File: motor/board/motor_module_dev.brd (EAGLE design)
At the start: 44.4 x 51.7 mm, 74 parts, among them IC6 LTC6088, IC7 DRV8833RTY

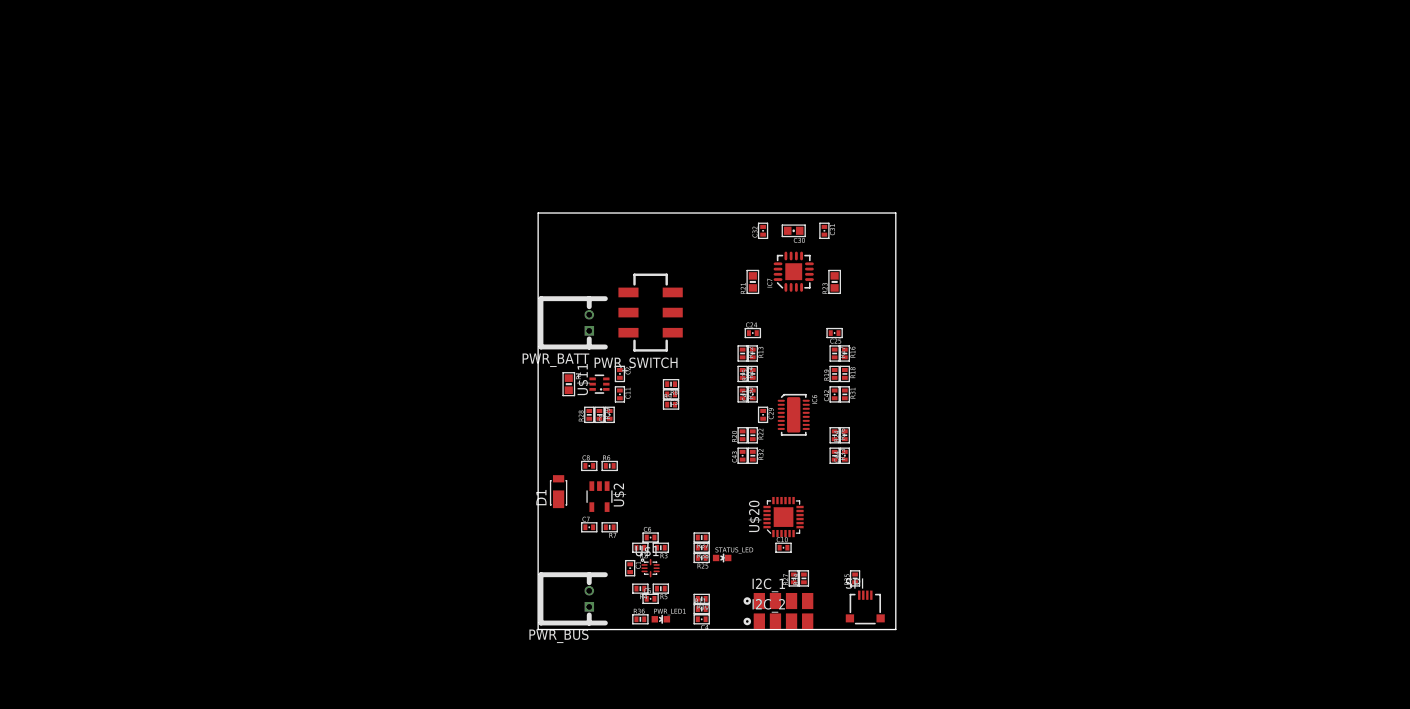
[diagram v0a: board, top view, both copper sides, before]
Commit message: Switched I2C and Charge pins for better Arduino compatability. Adding dev version
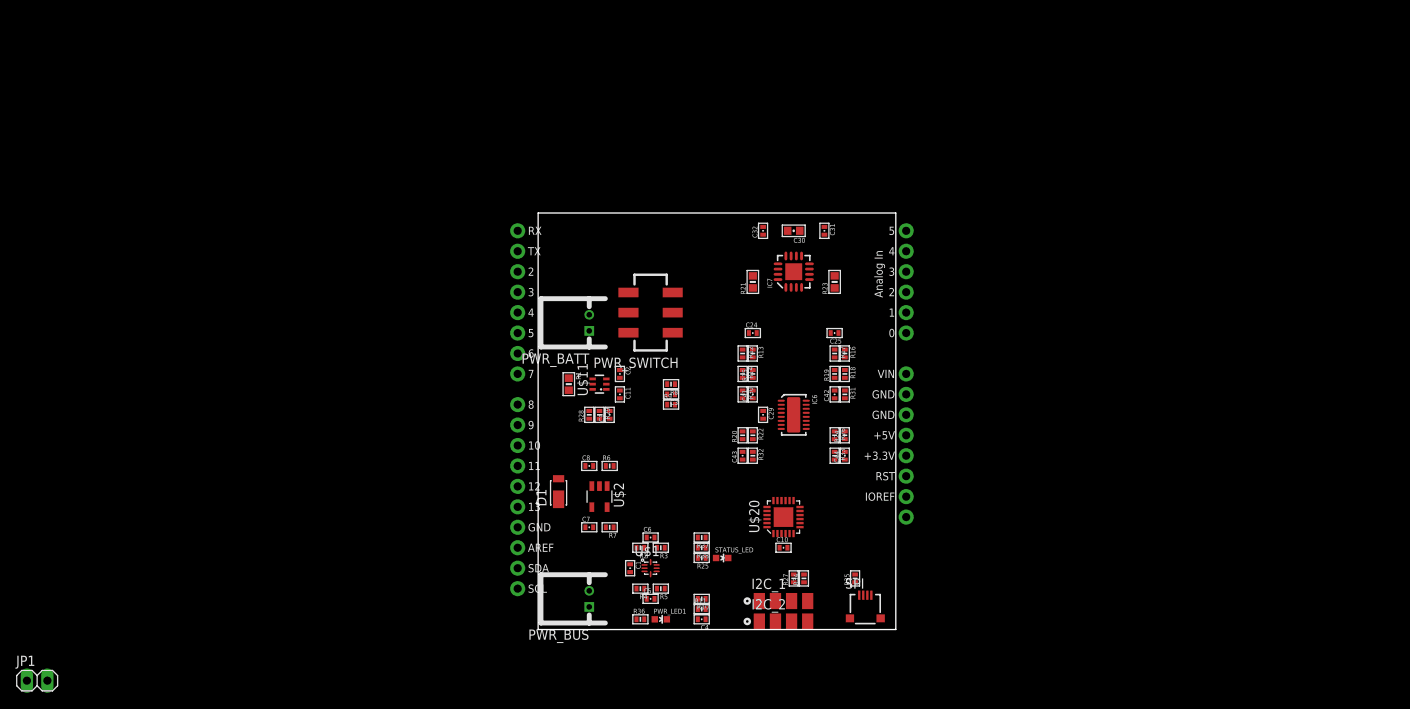
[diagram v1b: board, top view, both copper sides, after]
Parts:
- added JP1: (no value), pinhead:1X02
- added U$27: ARDUINO_R3_SHIELD, SparkFun-Boards:UNO_R3_SHIELD
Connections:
- new net N$10: JP1.2, U$27.5V
- net GND: now also U$27.GND@0, U$27.GND@1, U$27.GND@2
- net I2C_SCL: now also U$27.SCL
- net I2C_SDA: now also U$27.SDA
- net SPI_SS: now also U$27.D10
- net V_BUS: now also JP1.1
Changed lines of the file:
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@@
 <element name="R38" library="biomimetic" package="0402-RES" value="4.7k" x="20.32" y="10.16" rot="R180"/>
 <element name="C11" library="biomimetic" package="0402-CAP" value="100nF" x="10.16" y="29.21" rot="R270"/>
+<element name="U$27" library="SparkFun-Boards" package="UNO_R3_SHIELD" value="ARDUINO_R3_SHIELD" x="-5.08" y="-5.08"/>
+<element name="JP1" library="pinhead" package="1X02" value="" x="-62.23" y="-6.35"/>
 </elements>
 <signals>
@@
 <contactref element="I2C_2" pad="2"/>
 <contactref element="C11" pad="1"/>
+<contactref element="U$27" pad="GND@2"/>
+<contactref element="U$27" pad="GND@1"/>
+<contactref element="U$27" pad="GND@0"/>
 <wire x1="27.94" y1="50.0126" x2="31.0007" y2="49.53" width="0" layer="19" extent="1-1"/>
 <wire x1="31.425" y1="46.4" x2="31.0007" y2="49.53" width="0" layer="19" extent="1-1"/>
@@
 <wire x1="30.9626" y1="10.16" x2="29.48" y2="3.54" width="0" layer="19" extent="1-1"/>
 <wire x1="30.73" y1="11.92" x2="30.9626" y2="10.16" width="0" layer="19" extent="1-1"/>
+<wire x1="45.72" y1="26.67" x2="6.35" y2="37.1" width="0" layer="19" extent="1-1"/>
+<wire x1="45.72" y1="29.21" x2="45.72" y2="26.67" width="0" layer="19" extent="1-1"/>
+<wire x1="-2.54" y1="12.7" x2="45.72" y2="26.67" width="0" layer="19" extent="1-1"/>
 </signal>
 <signal name="N$1">
@@
 <contactref element="C1" pad="1"/>
 <contactref element="U$1" pad="6"/>
-<wire x1="14.72" y1="7.62" x2="19.8374" y2="3.81" width="0" layer="19" extent="1-1"/>
-<wire x1="13.22" y1="7.62" x2="14.72" y2="7.62" width="0" layer="19" extent="1-1"/>
-<wire x1="11.43" y1="8.1026" x2="13.22" y2="7.62" width="0" layer="19" extent="1-1"/>
+<contactref element="JP1" pad="1"/>
+<wire x1="2.54" y1="16.18" x2="-63.5" y2="-6.35" width="0" layer="19" extent="1-1"/>
+<wire x1="6.67" y1="15.204" x2="2.54" y2="16.18" width="0" layer="19" extent="1-1"/>
+<wire x1="5.8674" y1="12.7" x2="6.67" y2="15.204" width="0" layer="19" extent="1-1"/>
+<wire x1="11.43" y1="8.1026" x2="5.8674" y2="12.7" width="0" layer="19" extent="1-1"/>
+<wire x1="13.22" y1="7.62" x2="11.43" y2="8.1026" width="0" layer="19" extent="1-1"/>
+<wire x1="14.72" y1="7.62" x2="13.22" y2="7.62" width="0" layer="19" extent="1-1"/>
 <wire x1="6.35" y1="4.81" x2="11.43" y2="8.1026" width="0" layer="19" extent="1-1"/>
-<wire x1="5.8674" y1="12.7" x2="11.43" y2="8.1026" width="0" layer="19" extent="1-1"/>
-<wire x1="6.67" y1="15.204" x2="5.8674" y2="12.7" width="0" layer="19" extent="1-1"/>
-<wire x1="2.54" y1="16.18" x2="6.67" y2="15.204" width="0" layer="19" extent="1-1"/>
+<wire x1="19.8374" y1="3.81" x2="14.72" y2="7.62" width="0" layer="19" extent="1-1"/>
 </signal>
 <signal name="N$4">
@@
 <contactref element="I2C_1" pad="3"/>
 <contactref element="U$20" pad="17"/>
+<contactref element="U$27" pad="SCL"/>
 <wire x1="31.75" y1="5.8674" x2="29.73" y2="16.02" width="0" layer="19" extent="1-1"/>
 <wire x1="31.48" y1="3.54" x2="31.75" y2="5.8674" width="0" layer="19" extent="1-1"/>
 <wire x1="31.48" y1="1" x2="31.48" y2="3.54" width="0" layer="19" extent="1-1"/>
+<wire x1="-2.54" y1="5.08" x2="29.73" y2="16.02" width="0" layer="19" extent="1-1"/>
 </signal>
 <signal name="I2C_SDA">
@@
 <contactref element="R34" pad="1"/>
 <contactref element="U$20" pad="18"/>
+<contactref element="U$27" pad="SDA"/>
 <wire x1="33.02" y1="5.8674" x2="29.23" y2="16.02" width="0" layer="19" extent="1-1"/>
 <wire x1="33.48" y1="3.54" x2="33.02" y2="5.8674" width="0" layer="19" extent="1-1"/>
 <wire x1="33.48" y1="1" x2="33.48" y2="3.54" width="0" layer="19" extent="1-1"/>
+<wire x1="-2.54" y1="7.62" x2="29.23" y2="16.02" width="0" layer="19" extent="1-1"/>
 </signal>
 <signal name="SPI_SS">
@@
 <contactref element="SPI" pad="1"/>
 <contactref element="R35" pad="1"/>
+<contactref element="U$27" pad="D10"/>
 <wire x1="39.37" y1="5.8674" x2="32.53" y2="12.72" width="0" layer="19" extent="1-1"/>
 <wire x1="39.89" y1="4.265" x2="39.37" y2="5.8674" width="0" layer="19" extent="1-1"/>
+<wire x1="-2.54" y1="22.86" x2="32.53" y2="12.72" width="0" layer="19" extent="1-1"/>
 </signal>
 <signal name="SPI_MISO">
@@
 <wire x1="22.11" y1="8.89" x2="20.8026" y2="8.89" width="0" layer="19" extent="1-1"/>
 </signal>
+<signal name="N$10">
+<contactref element="U$27" pad="5V"/>
+<contactref element="JP1" pad="2"/>
+<wire x1="45.72" y1="24.13" x2="-60.96" y2="-6.35" width="0" layer="19" extent="1-1"/>
+</signal>
 </signals>

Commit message: Added parallel pull-up to status
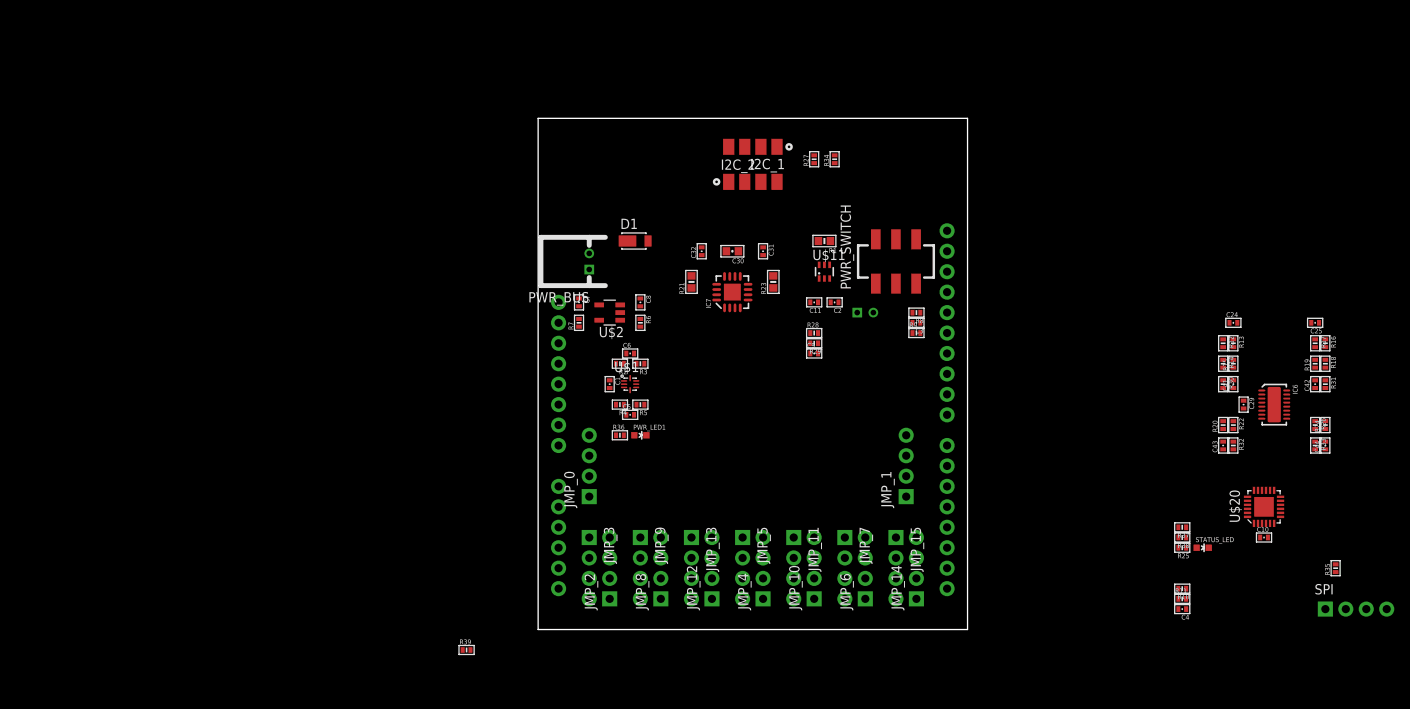
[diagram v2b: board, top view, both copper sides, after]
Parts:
- removed JP1: (no value), pinhead:1X02
- added JMP_0, JMP_1, JMP_10, JMP_11, JMP_12, JMP_13, JMP_14, JMP_15, JMP_2, JMP_3, JMP_4, JMP_5, JMP_6, JMP_7, JMP_8, JMP_9: (no value), modular_robotics:1X04_NO_SILK
- added R39: 4.7k, biomimetic:0402-RES
- SPI: device modular_robotics:MOLEX_503480-0400 -> modular_robotics:1X04_NO_SILK
- U$27: value ARDUINO_R3_SHIELD -> ARDUINO_R3_SHIELDNOLABELS; device SparkFun-Boards:UNO_R3_SHIELD -> SparkFun-Boards:UNO_R3_SHIELD_NOLABELS
- moved U$27 87.2 mm to (53.3, 59.7), turned to 180 degrees
- moved C4 59.7 mm to (80.0, 2.54)
- moved C43 59.7 mm to (85.1, 22.9)
- moved C44 59.7 mm to (97.8, 22.9)
- moved R10 59.7 mm to (80.0, 5.08)
- moved R11 59.7 mm to (80.0, 3.81)
- moved R12 59.7 mm to (85.1, 35.6)
- moved R14 59.7 mm to (85.1, 33.0)
- moved R16 59.7 mm to (97.8, 35.6)
- moved R18 59.7 mm to (97.8, 33.0)
- moved R20 59.7 mm to (85.1, 25.4)
- moved R24 59.7 mm to (97.8, 25.4)
- moved R25 59.7 mm to (80.0, 10.2)
- moved R30 59.7 mm to (85.1, 30.5)
- moved R31 59.7 mm to (97.8, 30.5)
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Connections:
- removed net N$10: JP1.2, U$27.5V
- new net ARD_5V: JMP_0.1, JMP_0.2, U$27.5V
- new net ARD_A0: JMP_10.1, JMP_10.2, JMP_7.3, JMP_7.4, U$27.A0
- new net ARD_A1: JMP_9.3, JMP_9.4, U$27.A1
- new net ARD_A2: JMP_3.3, JMP_3.4, U$27.A2
- new net ARD_A4: JMP_5.3, JMP_5.4, U$27.A4
- new net ARD_AREF: JMP_1.1, JMP_1.2, U$27.AREF
- new net ARD_D0-RX: JMP_11.3, JMP_11.4, JMP_4.1, JMP_4.2, U$27.RX
- new net ARD_D1-TX: JMP_2.1, JMP_2.2, U$27.TX
- new net ARD_D3: JMP_15.3, JMP_15.4, JMP_6.1, JMP_6.2, U$27.D3
- new net ARD_D5: JMP_13.3, JMP_13.4, JMP_8.1, JMP_8.2, U$27.D5
- new net ARD_D7: JMP_12.1, JMP_12.2, U$27.D7
- new net ARD_D8: JMP_14.1, JMP_14.2, U$27.D8
- net CHARGE_ENABLE: now also U$27.D4
- net CHARGE_STATUS: now also U$27.D2
- net MOTOR_A_BEMF: now also JMP_2.3, JMP_2.4, JMP_3.1, JMP_3.2
- net MOTOR_A_IN1: now also JMP_14.3, JMP_14.4, JMP_15.1, JMP_15.2
- net MOTOR_A_IN2: now also U$27.D9
- net MOTOR_B_BEMF: now also JMP_4.3, JMP_4.4, JMP_5.1, JMP_5.2
- net MOTOR_B_IN1: now also U$27.D6
- net MOTOR_B_IN2: now also JMP_12.3, JMP_12.4, JMP_13.1, JMP_13.2
- net RESET: now also U$27.RES
- net SENSE_I_BATT: now also JMP_8.3, JMP_8.4, JMP_9.1, JMP_9.2
- net SENSE_V_BATT: now also JMP_6.3, JMP_6.4, JMP_7.1, JMP_7.2
- net SENSE_V_BUS: now also U$27.A5
- net SPI_MISO: now also U$27.D12
- net SPI_MOSI: now also U$27.D11
- net SPI_SCK: now also U$27.D13
- net SWD_CLK: now also U$27.A3
- net SWD_DIO/STATUS: now also JMP_10.3, JMP_10.4, JMP_11.1, JMP_11.2, R39.1
- net V_3.0: now also JMP_1.3, JMP_1.4, R39.2
- net V_BUS: now also JMP_0.3, JMP_0.4; no longer JP1.1
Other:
- board size 44.4 x 51.7 mm -> 53.3 x 63.5 mm

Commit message: Working on layout
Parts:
- moved R25 70.8 mm to (10.2, 21.6)
- moved R37 70.8 mm to (10.2, 24.1)
- moved R38 70.8 mm to (10.2, 22.9)
- moved STATUS_LED 70.8 mm to (12.7, 21.6), turned to 180 degrees
- moved C4 68.9 mm to (16.5, 29.2)
- moved R10 68.9 mm to (16.5, 31.8)
- moved R11 68.9 mm to (16.5, 30.5)
- moved C10 62.7 mm to (27.9, 19.1)
- moved U$20 62.7 mm to (27.9, 22.9)
- moved R35 58.0 mm to (41.9, 17.8), turned to 0 degrees
- moved SPI 57.3 mm to (41.9, 15.2), turned to 180 degrees
- moved R39 29.8 mm to (10.2, 20.3), turned to 180 degrees
- moved PWR_LED1 10.9 mm to (6.35, 33.0), turned to 0 degrees
- moved R36 6.35 mm to (6.35, 29.2), turned to 90 degrees
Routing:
- added copper zone on layer 1, net GND

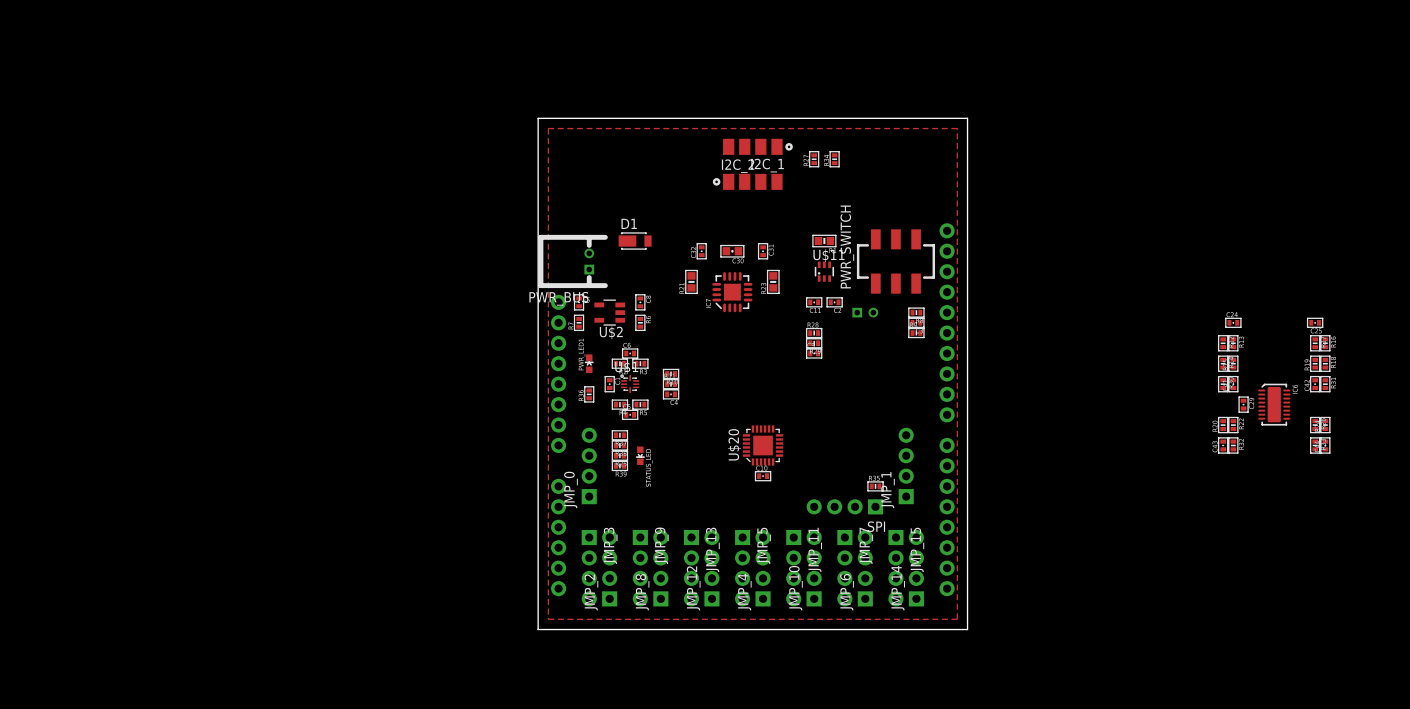
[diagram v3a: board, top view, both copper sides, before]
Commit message: Layout complete. Need to fix some crossing wires, tidy up, figure out if need to fix A4/A2 connection issue.
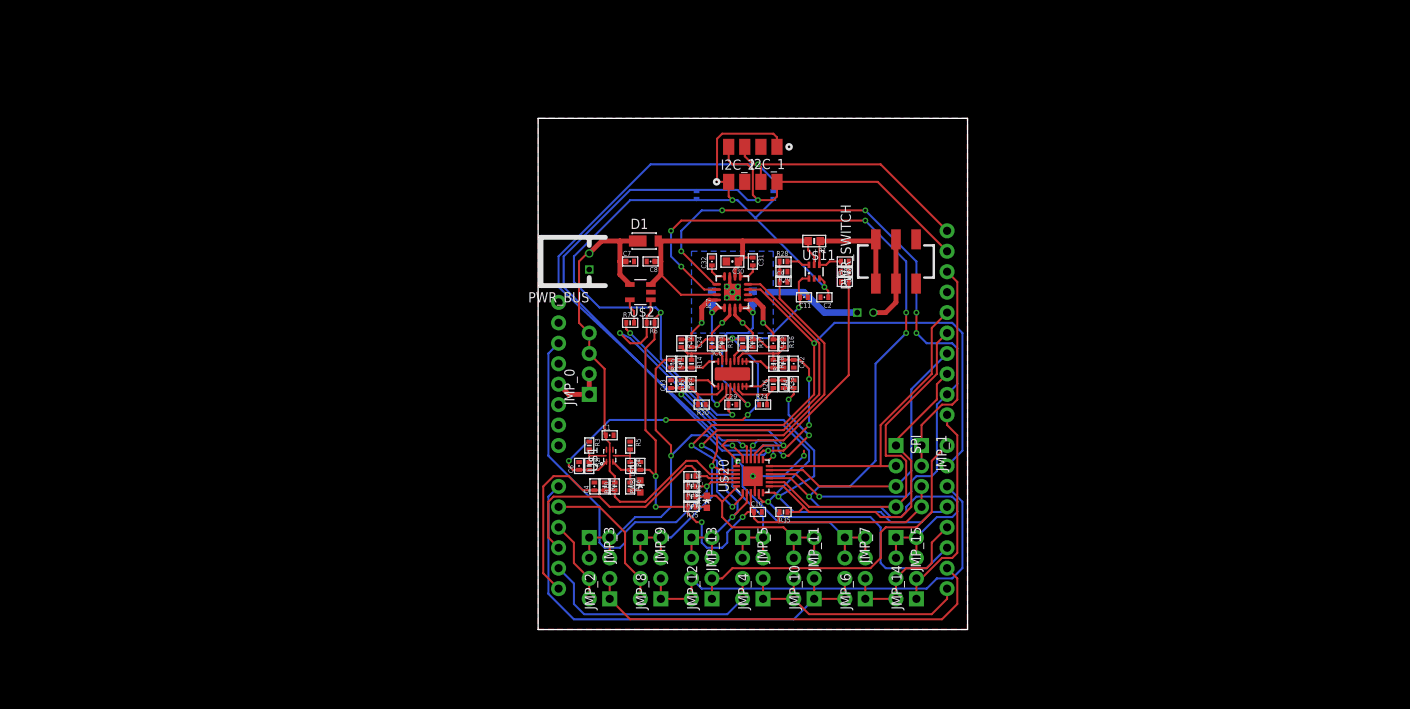
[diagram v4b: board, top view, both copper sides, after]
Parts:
- moved R19 71.2 mm to (25.4, 35.6), turned to 270 degrees
- moved R24 69.9 mm to (27.9, 27.9), turned to 0 degrees
- moved C41 69.9 mm to (16.5, 33.0), turned to 270 degrees
- moved R17 69.8 mm to (26.7, 35.6)
- moved C43 69.0 mm to (16.5, 30.5)
- moved R32 69.0 mm to (17.8, 30.5)
- moved R18 68.6 mm to (29.2, 33.0)
- moved R22 67.5 mm to (19.1, 30.5), turned to 90 degrees
- moved R26 67.5 mm to (29.2, 30.5), turned to 90 degrees
- moved IC6 67.4 mm to (24.1, 31.8), turned to 0 degrees
- moved C24 67.4 mm to (19.1, 35.6), turned to 270 degrees
- moved C25 67.4 mm to (29.2, 35.6), turned to 270 degrees
- moved R30 67.4 mm to (17.8, 33.0), turned to 90 degrees
- moved R31 67.4 mm to (30.5, 33.0), turned to 90 degrees
- moved R12 67.3 mm to (17.8, 35.6)
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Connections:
- net MOTOR_A_ISEN: now also IC6.3; no longer IC6.5
- net MOTOR_B_ISEN: now also IC6.5; no longer IC6.12
- net N$22: now also IC6.11; no longer IC6.15
- net N$23: now also IC6.12; no longer IC6.14
- net N$24: now also IC6.2; no longer IC6.6
- net N$26: now also IC6.6; no longer IC6.11
- net N$30: now also IC6.15; no longer IC6.2
- net N$31: now also IC6.14; no longer IC6.3
- net N$34: now also IC6.7; no longer IC6.10
- net N$35: now also IC6.1; no longer IC6.7
- net N$36: now also IC6.16; no longer IC6.1
- net N$37: now also IC6.10; no longer IC6.16
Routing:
- net V_3.0: track 0.00 -> 184.6 mm, vias 0 -> 8
- net MOTOR_A_IN1: track 0.00 -> 121.2 mm, vias 0 -> 6
- net I2C_SCL: track 0.00 -> 102.7 mm, vias 0 -> 2
- net I2C_SDA: track 0.00 -> 101.7 mm, vias 0 -> 2
- net MOTOR_A_IN2: track 0.00 -> 96.6 mm, vias 0 -> 6
- net MOTOR_B_IN1: track 0.00 -> 85.0 mm, vias 0 -> 3
- net CHARGE_STATUS: track 0.00 -> 78.2 mm, vias 0 -> 2
- net CHARGE_ENABLE: track 0.00 -> 63.9 mm, vias 0 -> 2
- net SENSE_V_BATT: track 0.00 -> 63.3 mm, vias 0 -> 1
- net MOTOR_B_IN2: track 0.00 -> 61.5 mm, vias 0 -> 2
- net SENSE_I_BATT: track 0.00 -> 61.2 mm, vias 0 -> 1
- net V_1.5: track 0.00 -> 59.1 mm, vias 0 -> 5
- net ARD_A0: track 0.00 -> 58.1 mm
- net MOTOR_A_BEMF: track 0.00 -> 56.0 mm, vias 0 -> 2
- net ARD_D5: track 0.00 -> 55.1 mm
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- added copper zone on layer 16, net GND
